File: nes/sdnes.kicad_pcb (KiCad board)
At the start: 2 copper layers, 17.8 x 22.4 mm, 5 parts, among them J2 500901-0801

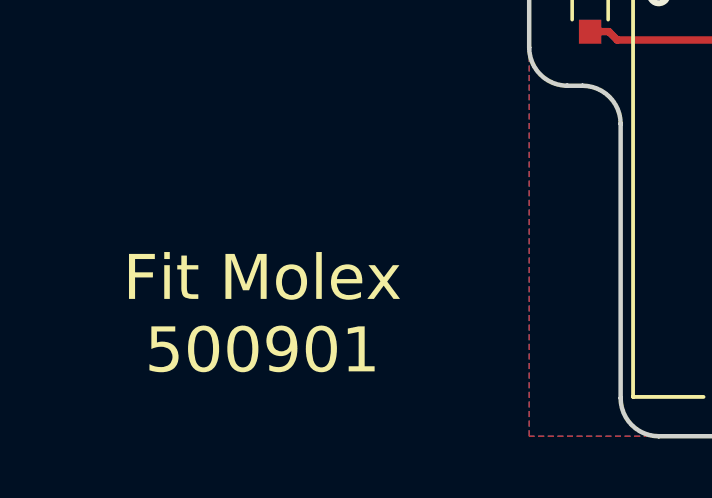
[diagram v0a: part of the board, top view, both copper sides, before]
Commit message: Fix silkscreen
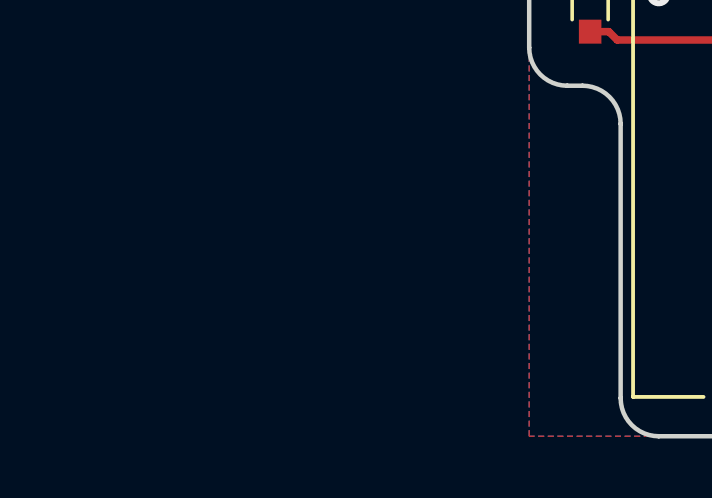
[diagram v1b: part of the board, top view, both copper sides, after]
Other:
- board text added: "SDNES SHVC github.com/ going-digital /sdnes"
- board text removed: "SD mod for FTM-NES- Main-01 by Cathedrow"
- board text removed: "SD mod for FTM-SHVC- Main-01 by Cathedrow"
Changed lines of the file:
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@@
   (general
     (thickness 0.8)
-    (drawings 16)
+    (drawings 14)
     (tracks 90)
     (zones 0)
@@
   (layers
     (0 F.Cu signal)
-    (31 B.Cu signal)
+    (31 B.Cu signal hide)
     (32 B.Adhes user hide)
     (33 F.Adhes user hide)
     (34 B.Paste user hide)
     (35 F.Paste user hide)
-    (36 B.SilkS user hide)
-    (37 F.SilkS user hide)
+    (36 B.SilkS user)
+    (37 F.SilkS user)
     (38 B.Mask user)
     (39 F.Mask user hide)
@@
       (drillshape 0)
       (scaleselection 1)
-      (outputdirectory "./"))
+      (outputdirectory "fabrication/"))
   )
   (net 0 "")
@@
     )
   )
-  (gr_text "SD mod for\nFTM-SHVC-\nMain-01\nby\nCathedrow" (at 149.352 104.14) (layer B.SilkS)
-    (effects (font (size 1.5 1.5) (thickness 0.3)) (justify mirror))
-  )
-  (gr_text "SD mod for\nFTM-NES-\nMain-01\nby\nCathedrow" (at 168.656 102.108) (layer B.SilkS)
-    (effects (font (size 1.5 1.5) (thickness 0.3)) (justify mirror))
+  (gr_text "SDNES SHVC\ngithub.com/\ngoing-digital\n/sdnes" (at 168.656 103) (layer B.SilkS)
+    (effects (font (size 1.5 1.3) (thickness 0.3)) (justify mirror))
   )
   (gr_text "Fit Molex\n500901" (at 166.624 102.616 90) (layer F.SilkS)
-    (effects (font (size 1.5 1.5) (thickness 0.3)))
-  )
-  (gr_text "Fit Molex\n500901" (at 149.352 106.426) (layer F.SilkS)
     (effects (font (size 1.5 1.5) (thickness 0.3)))
   )
@@
   (gr_line (start 176.022 89.408) (end 176.022 109.22) (layer Edge.Cuts) (width 0.15))
   (gr_line (start 159.512 88.138) (end 174.752 88.138) (layer Edge.Cuts) (width 0.15))
+  (segment (start 173.99 90.4) (end 174.22 90.17) (width 0.25) (layer F.Cu) (net 1))
+  (segment (start 173.99 91.656) (end 173.99 90.4) (width 0.25) (layer F.Cu) (net 1))
   (segment (start 171.054 90.718) (end 171.054 90.79) (width 0.25) (layer B.Cu) (net 2))
   (segment (start 171.054 90.718) (end 171.054 90.79) (width 0.25) (layer F.Cu) (net 2))
@@
   (segment (start 174.498 88.9) (end 175.006 89.408) (width 0.25) (layer B.Cu) (net 9))
   (segment (start 172.08641 88.9) (end 174.498 88.9) (width 0.25) (layer B.Cu) (net 9))
-  (segment (start 173.99 90.4) (end 174.22 90.17) (width 0.25) (layer F.Cu) (net 1))
-  (segment (start 173.99 91.656) (end 173.99 90.4) (width 0.25) (layer F.Cu) (net 1))
   (zone (net 7) (net_name /0V) (layer B.Cu) (hatch edge 0.508)
     (connect_pads (clearance 0.508))

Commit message: Fix silkscreen
Fixes issue 1
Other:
- board text added: "SDNES NES github.com/ going-digital /sdnes"
- board text removed: "SDNES SHVC github.com/ going-digital /sdnes"
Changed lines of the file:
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@@
     )
   )
-  (gr_text "SDNES SHVC\ngithub.com/\ngoing-digital\n/sdnes" (at 168.656 103) (layer B.SilkS)
+  (gr_text "SDNES NES\ngithub.com/\ngoing-digital\n/sdnes" (at 168.656 103) (layer B.SilkS)
     (effects (font (size 1.5 1.3) (thickness 0.3)) (justify mirror))
   )

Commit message: Revert "Fix silkscreen"
This reverts commit b91a6601b2e49d2b5b00c3b97c6f2e9545f83911.
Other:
- board text added: "SDNES SHVC github.com/ going-digital /sdnes"
- board text removed: "SDNES NES github.com/ going-digital /sdnes"
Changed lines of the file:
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@@
     )
   )
-  (gr_text "SDNES NES\ngithub.com/\ngoing-digital\n/sdnes" (at 168.656 103) (layer B.SilkS)
+  (gr_text "SDNES SHVC\ngithub.com/\ngoing-digital\n/sdnes" (at 168.656 103) (layer B.SilkS)
     (effects (font (size 1.5 1.3) (thickness 0.3)) (justify mirror))
   )
